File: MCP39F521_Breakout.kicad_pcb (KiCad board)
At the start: 2 copper layers, 35.6 x 27.9 mm, 32 parts, among them J1 TEST_1P, J10 Conn_01x01, J11 Conn_01x10, J2 Conn_01x01, J3 Conn_01x01, J4 Conn_01x01, J5 Conn_01x01, J6 TEST_1P, J7 TEST_1P, J8 Conn_01x01, J9 Conn_01x01, U1 MCP39F521

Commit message: More wiring
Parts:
- added R11: 2.4R, Resistor_SMD:R_0603_1608Metric, F.Cu at (127.6, 118.1)
- added R12: 2.4R, Resistor_SMD:R_0603_1608Metric, F.Cu at (123.8, 118.1)
- moved J11 0.25 mm to (120.7, 122.6)
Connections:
- net Net-(J11-Pad5) renamed PWM
- C1 pad 1: Net-(C1-Pad1) -> VN
- C2 pad 2: Net-(C2-Pad2) -> VP
- J11 pad 1: Net-(J11-Pad1) -> +3V3
- J11 pad 10: Net-(J11-Pad10) -> GNDD
- J11 pad 2: Net-(J11-Pad2) -> VP
- J11 pad 3: Net-(J11-Pad3) -> VN
- J11 pad 4: Net-(J11-Pad4) -> ~RESET
- J11 pad 6: Net-(J11-Pad6) -> SCL
- J11 pad 7: Net-(J11-Pad7) -> SDA
- J11 pad 8: Net-(J11-Pad8) -> IP
- J11 pad 9: Net-(J11-Pad9) -> IN
- L1 pad 2: Net-(L1-Pad2) -> IP
- L2 pad 2: Net-(L2-Pad2) -> IN
- R1 pad 1: Net-(C1-Pad1) -> VN
- R10 pad 2: Net-(R10-Pad2) -> SDA
- R2 pad 2: Net-(C2-Pad2) -> VP
- R5 pad 2: Net-(R5-Pad2) -> ~RESET
- R9 pad 2: Net-(R9-Pad2) -> SCL
- U1 pad 10: Net-(R5-Pad2) -> ~RESET
- U1 pad 13: Net-(R9-Pad2) -> SCL
- U1 pad 14: Net-(R10-Pad2) -> SDA
- U1 pad 18: Net-(C1-Pad1) -> VN
- U1 pad 19: Net-(C2-Pad2) -> VP

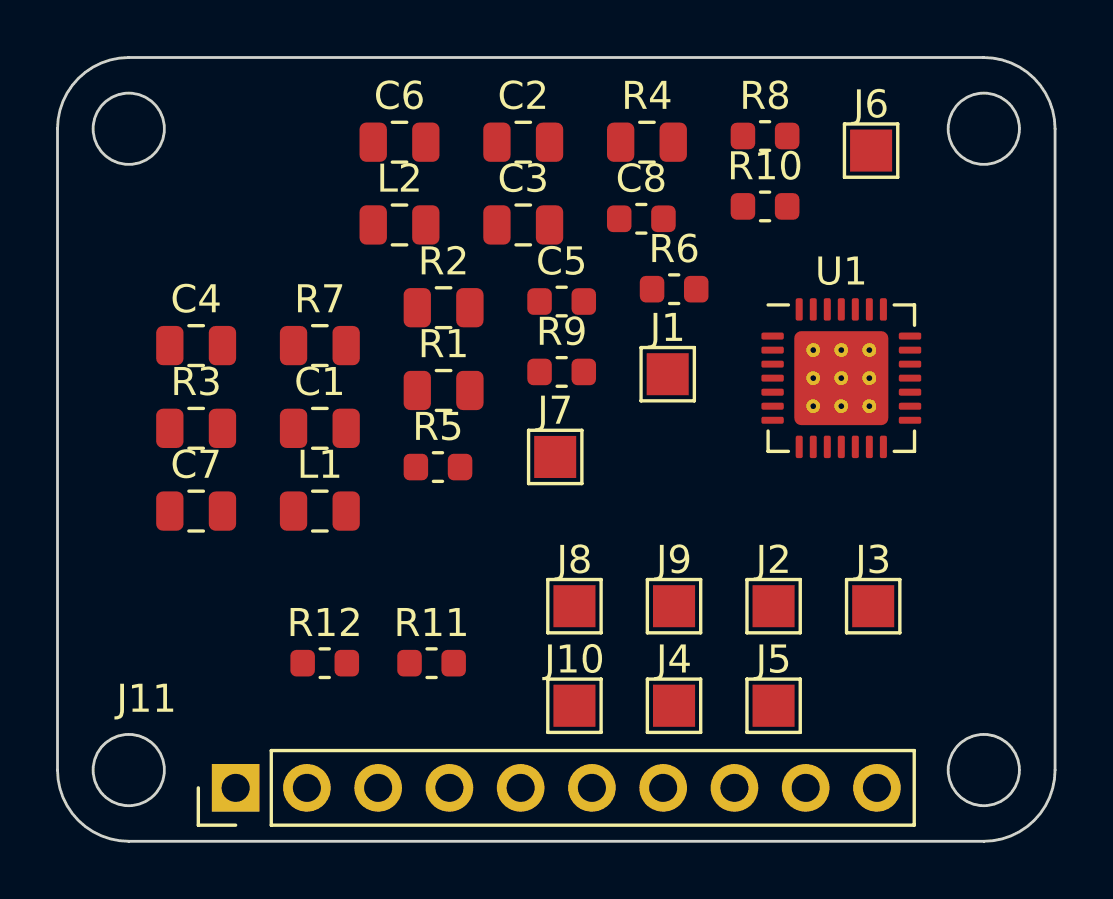
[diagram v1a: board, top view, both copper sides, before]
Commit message: Add address jumpers
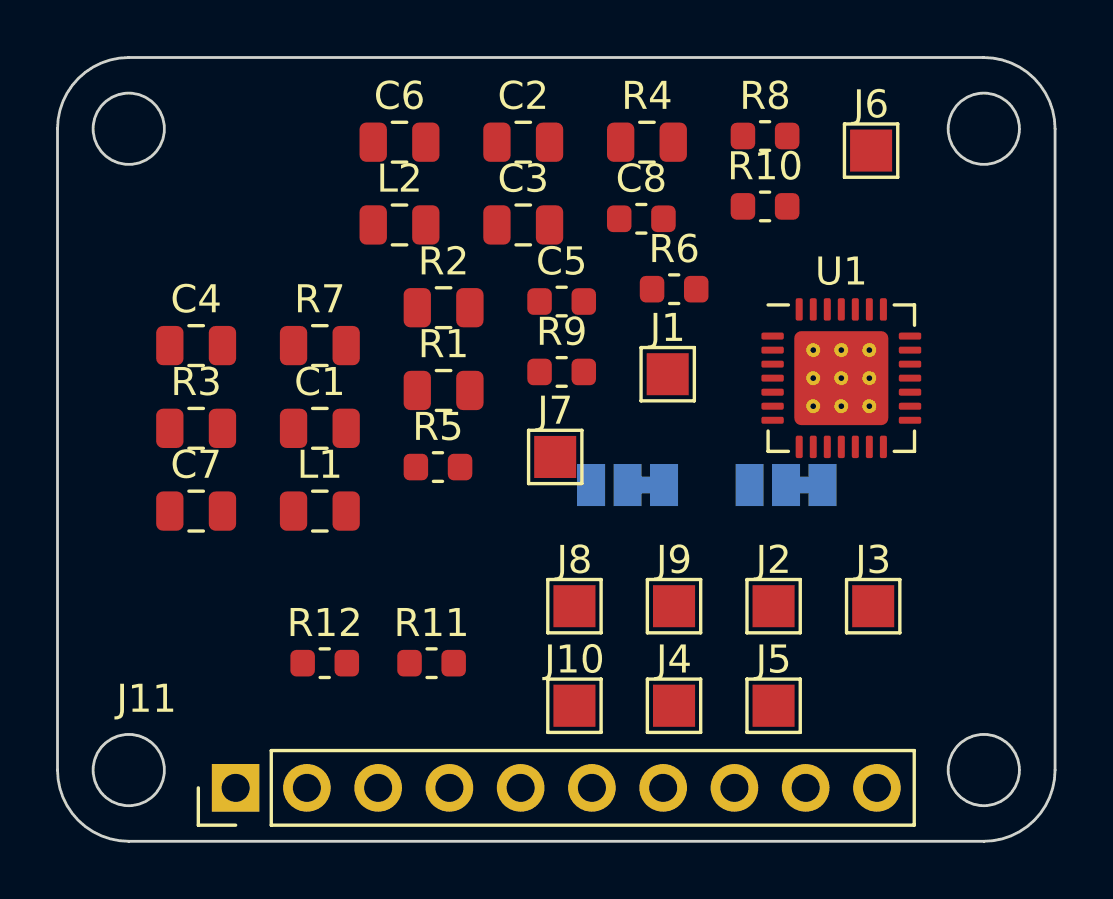
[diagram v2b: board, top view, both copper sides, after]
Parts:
- added A0: SolderJumper_3_Bridged12, Jumper:SolderJumper-3_P1.3mm_Bridged12_Pad1.0x1.5mm, B.Cu at (140.3, 111.8)
- added A1: SolderJumper_3_Bridged12, Jumper:SolderJumper-3_P1.3mm_Bridged12_Pad1.0x1.5mm, B.Cu at (134.6, 111.8)
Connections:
- U1 pad 12: GNDD -> /A0
- U1 pad 15: GNDD -> /A1
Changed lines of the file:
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@@
   (net 23 "+3V3")
   (net 24 "+3.3VA")
+  (net 25 "/A0")
+  (net 26 "/A1")
   (footprint "Resistor_SMD:R_0805_2012Metric" (layer "F.Cu")
     (at 135.312 99.539)
@@
       (net 24 "+3.3VA") (pinfunction "AVDD"))
     (pad "12" smd roundrect (at 0.5 2.45) (size 0.25 0.8) (layers "F.Cu" "F.Paste" "F.Mask") (roundrect_rratio 0.25)
-      (net 20 "GNDD") (pinfunction "A0"))
+      (net 25 "/A0") (pinfunction "A0"))
     (pad "13" smd roundrect (at 1 2.45) (size 0.25 0.8) (layers "F.Cu" "F.Paste" "F.Mask") (roundrect_rratio 0.25)
       (net 14 "SCL") (pinfunction "SCL"))
@@
       (net 13 "SDA") (pinfunction "SDA"))
     (pad "15" smd roundrect (at 2.45 1.5) (size 0.8 0.25) (layers "F.Cu" "F.Paste" "F.Mask") (roundrect_rratio 0.25)
-      (net 20 "GNDD") (pinfunction "A1"))
+      (net 26 "/A1") (pinfunction "A1"))
     (pad "16" smd roundrect (at 2.45 1) (size 0.8 0.25) (layers "F.Cu" "F.Paste" "F.Mask") (roundrect_rratio 0.25)
       (net 19 "Net-(C3-Pad1)") (pinfunction "I1+"))
@@
       (net 8 "Net-(J8-Pad1)") (pinfunction "Pin_1"))
   )
+  (footprint "Jumper:SolderJumper-3_P1.3mm_Bridged12_Pad1.0x1.5mm" (layer "B.Cu")
+    (at 134.62 111.76 180)
+    (descr "SMD Solder 3-pad Jumper, 1x1.5mm Pads, 0.3mm gap, pads 1-2 bridged with 1 copper strip")
+    (tags "solder jumper open")
+    (property "Sheet file" "MCP39F521_Breakout.kicad_sch")
+    (property "Sheet name" "")
+    (attr exclude_from_pos_files)
+    (fp_text reference "A1" (at 0 1.8) (layer "B.SilkS")
+      (effects (font (size 1 1) (thickness 0.15)) (justify mirror))
+    )
+    (fp_text value "SolderJumper_3_Bridged12" (at 0 -2) (layer "B.Fab")
+      (effects (font (size 1 1) (thickness 0.15)) (justify mirror))
+    )
+    (fp_poly (pts (xy -0.9 0.3)
+      (xy -0.4 0.3)
+      (xy -0.4 -0.3)
+      (xy -0.9 -0.3)) (layer "B.Cu") (width 0) (fill solid))
+    (fp_line (start 2.05 1) (end 2.05 -1) (layer "B.SilkS") (width 0.12))
+    (fp_line (start -1.6 -1.5) (end -1 -1.5) (layer "B.SilkS") (width 0.12))
+    (fp_line (start -1.3 -1.2) (end -1 -1.5) (layer "B.SilkS") (width 0.12))
+    (fp_line (start -2.05 -1) (end -2.05 1) (layer "B.SilkS") (width 0.12))
+    (fp_line (start -1.3 -1.2) (end -1.6 -1.5) (layer "B.SilkS") (width 0.12))
+    (fp_line (start -2.05 1) (end 2.05 1) (layer "B.SilkS") (width 0.12))
+    (fp_line (start 2.05 -1) (end -2.05 -1) (layer "B.SilkS") (width 0.12))
+    (fp_line (start -2.3 1.25) (end 2.3 1.25) (layer "B.CrtYd") (width 0.05))
+    (fp_line (start -2.3 1.25) (end -2.3 -1.25) (layer "B.CrtYd") (width 0.05))
+    (fp_line (start 2.3 -1.25) (end -2.3 -1.25) (layer "B.CrtYd") (width 0.05))
+    (fp_line (start 2.3 -1.25) (end 2.3 1.25) (layer "B.CrtYd") (width 0.05))
+    (pad "1" smd rect (at -1.3 0 180) (size 1 1.5) (layers "B.Cu" "B.Mask")
+      (net 20 "GNDD") (pinfunction "A"))
+    (pad "2" smd rect (at 0 0 180) (size 1 1.5) (layers "B.Cu" "B.Mask")
+      (net 26 "/A1") (pinfunction "C"))
+    (pad "3" smd rect (at 1.3 0 180) (size 1 1.5) (layers "B.Cu" "B.Mask")
+      (net 23 "+3V3") (pinfunction "B"))
+  )
+  (footprint "Jumper:SolderJumper-3_P1.3mm_Bridged12_Pad1.0x1.5mm" (layer "B.Cu")
+    (at 140.27 111.76 180)
+    (descr "SMD Solder 3-pad Jumper, 1x1.5mm Pads, 0.3mm gap, pads 1-2 bridged with 1 copper strip")
+    (tags "solder jumper open")
+    (property "Sheet file" "MCP39F521_Breakout.kicad_sch")
+    (property "Sheet name" "")
+    (attr exclude_from_pos_files)
+    (fp_text reference "A0" (at 0 1.8) (layer "B.SilkS")
+      (effects (font (size 1 1) (thickness 0.15)) (justify mirror))
+    )
+    (fp_text value "SolderJumper_3_Bridged12" (at 0 -2) (layer "B.Fab")
+      (effects (font (size 1 1) (thickness 0.15)) (justify mirror))
+    )
+    (fp_poly (pts (xy -0.9 0.3)
+      (xy -0.4 0.3)
+      (xy -0.4 -0.3)
+      (xy -0.9 -0.3)) (layer "B.Cu") (width 0) (fill solid))
+    (fp_line (start -1.3 -1.2) (end -1.6 -1.5) (layer "B.SilkS") (width 0.12))
+    (fp_line (start -2.05 1) (end 2.05 1) (layer "B.SilkS") (width 0.12))
+    (fp_line (start -1.3 -1.2) (end -1 -1.5) (layer "B.SilkS") (width 0.12))
+    (fp_line (start 2.05 1) (end 2.05 -1) (layer "B.SilkS") (width 0.12))
+    (fp_line (start -2.05 -1) (end -2.05 1) (layer "B.SilkS") (width 0.12))
+    (fp_line (start 2.05 -1) (end -2.05 -1) (layer "B.SilkS") (width 0.12))
+    (fp_line (start -1.6 -1.5) (end -1 -1.5) (layer "B.SilkS") (width 0.12))
+    (fp_line (start -2.3 1.25) (end 2.3 1.25) (layer "B.CrtYd") (width 0.05))
+    (fp_line (start 2.3 -1.25) (end -2.3 -1.25) (layer "B.CrtYd") (width 0.05))
+    (fp_line (start -2.3 1.25) (end -2.3 -1.25) (layer "B.CrtYd") (width 0.05))
+    (fp_line (start 2.3 -1.25) (end 2.3 1.25) (layer "B.CrtYd") (width 0.05))
+    (pad "1" smd rect (at -1.3 0 180) (size 1 1.5) (layers "B.Cu" "B.Mask")
+      (net 20 "GNDD") (pinfunction "A"))
+    (pad "2" smd rect (at 0 0 180) (size 1 1.5) (layers "B.Cu" "B.Mask")
+      (net 25 "/A0") (pinfunction "C"))
+    (pad "3" smd rect (at 1.3 0 180) (size 1 1.5) (layers "B.Cu" "B.Mask")
+      (net 23 "+3V3") (pinfunction "B"))
+  )
   (gr_arc (start 116.84 99.06) (end 116.84 96.52) (angle -90) (layer "Edge.Cuts") (width 0.1))

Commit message: Cleanup copy-pasted symbols and perform initial autoroute
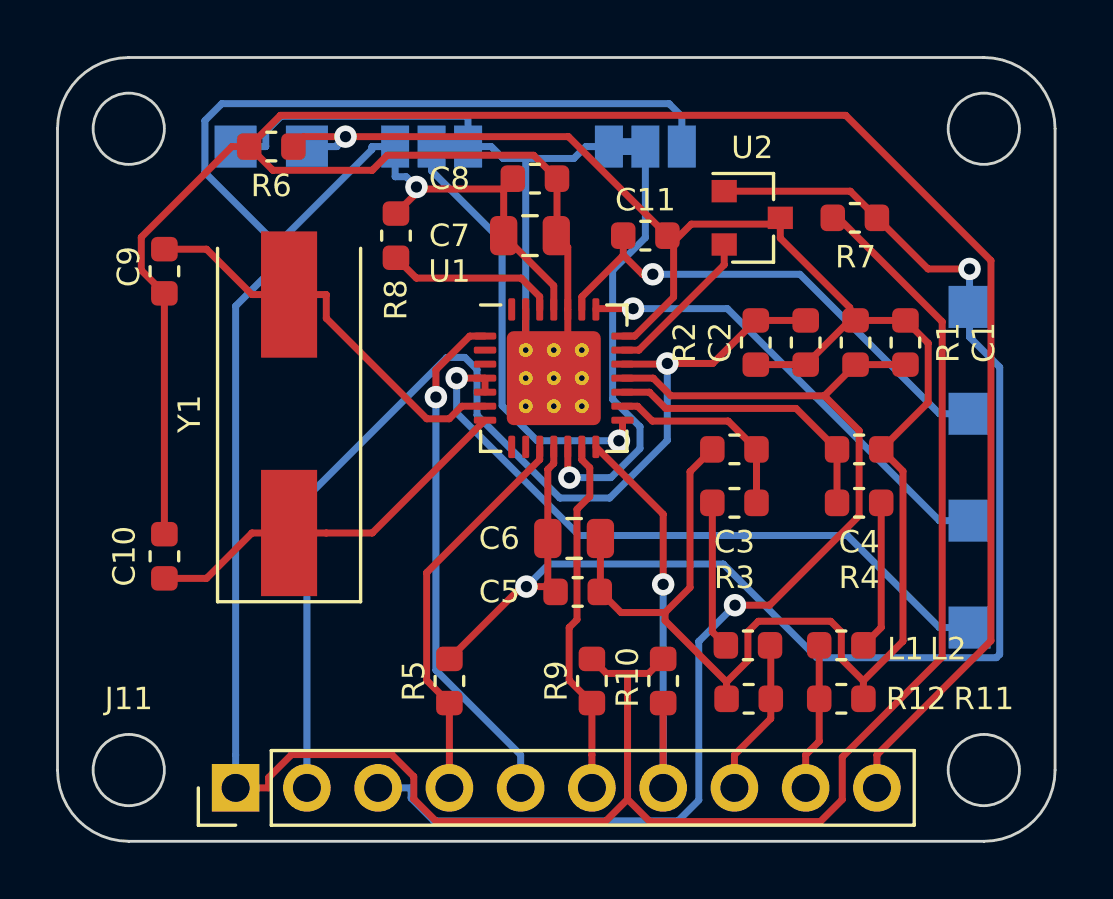
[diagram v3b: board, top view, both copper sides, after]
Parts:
- removed J10, J3: Conn_01x01, TestPoint:TestPoint_Pad_1.5x1.5mm
- removed the J4 at (136.3, 119.6)
- removed the J5 at (139.8, 119.6)
- added C10: 22pF, Capacitor_SMD:C_0603_1608Metric, F.Cu at (118.1, 114.3)
- added C11: 0.1uF 25V, Capacitor_SMD:C_0603_1608Metric, F.Cu at (135.3, 102.9)
- added C9: 22pF, Capacitor_SMD:C_0603_1608Metric, F.Cu at (118.1, 104.1)
- added U2: MCP9700AT-ETT, Package_TO_SOT_SMD:SOT-23, F.Cu at (139.1, 102.2)
- added Y1: Crystal, Crystal:Crystal_SMD_HC49-SD, F.Cu at (122.6, 109.2)
- C1, C2, C3, C4: footprint Capacitor_SMD:C_0805_2012Metric -> Capacitor_SMD:C_0603_1608Metric
- J2: moved to B.Cu
- J4: renamed from J8; moved to B.Cu
- J5: renamed from J9; moved to B.Cu
- L1, L2: footprint Inductor_SMD:L_0805_2012Metric -> Inductor_SMD:L_0603_1608Metric
- R1, R2, R3, R4, R7: footprint Resistor_SMD:R_0805_2012Metric -> Resistor_SMD:R_0603_1608Metric
- TP1: renamed from J1; value TEST_1P -> TestPoint; moved to B.Cu
- TP2: renamed from J6; value TEST_1P -> TestPoint; moved to B.Cu
- TP3: renamed from J7; value TEST_1P -> TestPoint; moved to B.Cu
- moved C4 23.9 mm to (142.9, 110.5), turned to 180 degrees
- moved L2 21.7 mm to (142.2, 117.5), turned to 180 degrees
- moved C1 21.1 mm to (144.5, 106.7), turned to 90 degrees
- moved TP2 20.1 mm to (123.2, 99.7), turned to 180 degrees
- moved R7 19.6 mm to (142.7, 102.2)
- moved R3 19.4 mm to (138.4, 112.4), turned to 180 degrees
- moved R10 17.3 mm to (135.9, 118.7), turned to -90 degrees
- moved L1 16.0 mm to (138.9, 117.5)
- moved TP3 15.9 mm to (120.7, 99.7), turned to 180 degrees
- moved C6 15.4 mm to (132.7, 113.7)
- moved C7 15.4 mm to (131.1, 102.9)
- moved R6 15.2 mm to (121.9, 99.7)
- moved R12 15.2 mm to (138.9, 119.4)
- moved R4 14.9 mm to (142.9, 112.4)
- moved R1 14.8 mm to (142.7, 106.7), turned to 90 degrees
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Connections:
- net Net-(C3-Pad1) renamed /I1+
- net Net-(C4-Pad2) renamed /I1-
- net Net-(J2-Pad1) renamed /REF_IN
- J11 pad 5: PWM -> EVENT
- U1 pad 1: Net-(J10-Pad1) -> EVENT
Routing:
- net +3V3: track 0.00 -> 117.7 mm, vias 0 -> 1
- net GNDD: track 0.00 -> 115.5 mm
- net GNDA: track 0.00 -> 74.2 mm, vias 0 -> 1
- net +3.3VA: track 0.00 -> 52.7 mm, vias 0 -> 2
- net VN: track 0.00 -> 41.3 mm, vias 0 -> 1
- net VP: track 0.00 -> 39.1 mm, vias 0 -> 1
- net Net-(J5-Pad1): track 0.00 -> 24.2 mm, vias 0 -> 1
- net EVENT: track 0.00 -> 18.4 mm, vias 0 -> 1
- net /REF_IN: track 0.00 -> 17.9 mm, vias 0 -> 1
- net Net-(J4-Pad1): track 0.00 -> 16.5 mm, vias 0 -> 1
- net SDA: track 0.00 -> 16.2 mm, vias 0 -> 1
- net /A1: track 0.00 -> 15.7 mm, vias 0 -> 1
- net /A0: track 0.00 -> 15.7 mm, vias 0 -> 1
- net Net-(C9-Pad1): track 0.00 -> 14.6 mm
- net ~RESET: track 0.00 -> 14.2 mm
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
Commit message: Clean-up initial route and setup net-classes
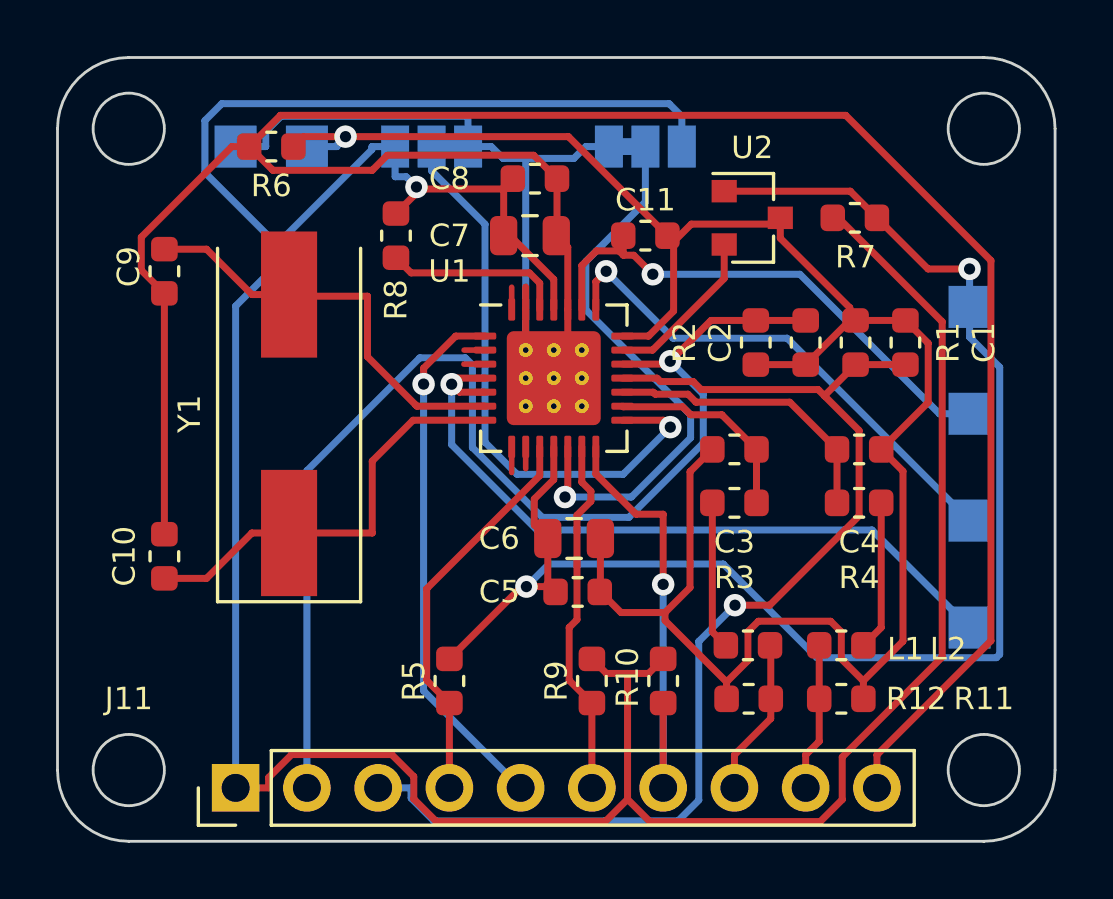
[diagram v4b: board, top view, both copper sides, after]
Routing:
- net GNDD: track 115.5 -> 107.9 mm
- net /A1: track 15.7 -> 20.9 mm
- net /A0: track 15.7 -> 20.0 mm
- net (no net): track 0.00 -> 3.98 mm
- net VP: track 39.1 -> 42.9 mm
- net Net-(J5-Pad1): track 24.2 -> 25.9 mm
- net Net-(J4-Pad1): track 16.5 -> 18.1 mm
- net Net-(C10-Pad1): track 13.8 -> 15.3 mm
- net /REF_IN: track 17.9 -> 18.7 mm
- net EVENT: track 18.4 -> 19.1 mm
- net SDA: track 16.2 -> 16.7 mm
